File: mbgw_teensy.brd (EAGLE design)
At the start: 49 x 42 mm, 39 parts, among them IC1 MAX481CSA, Q1 MOSFET-N2N7002, Q2 MOSFET-N2N7002, Q3 MOSFET-N2N7002

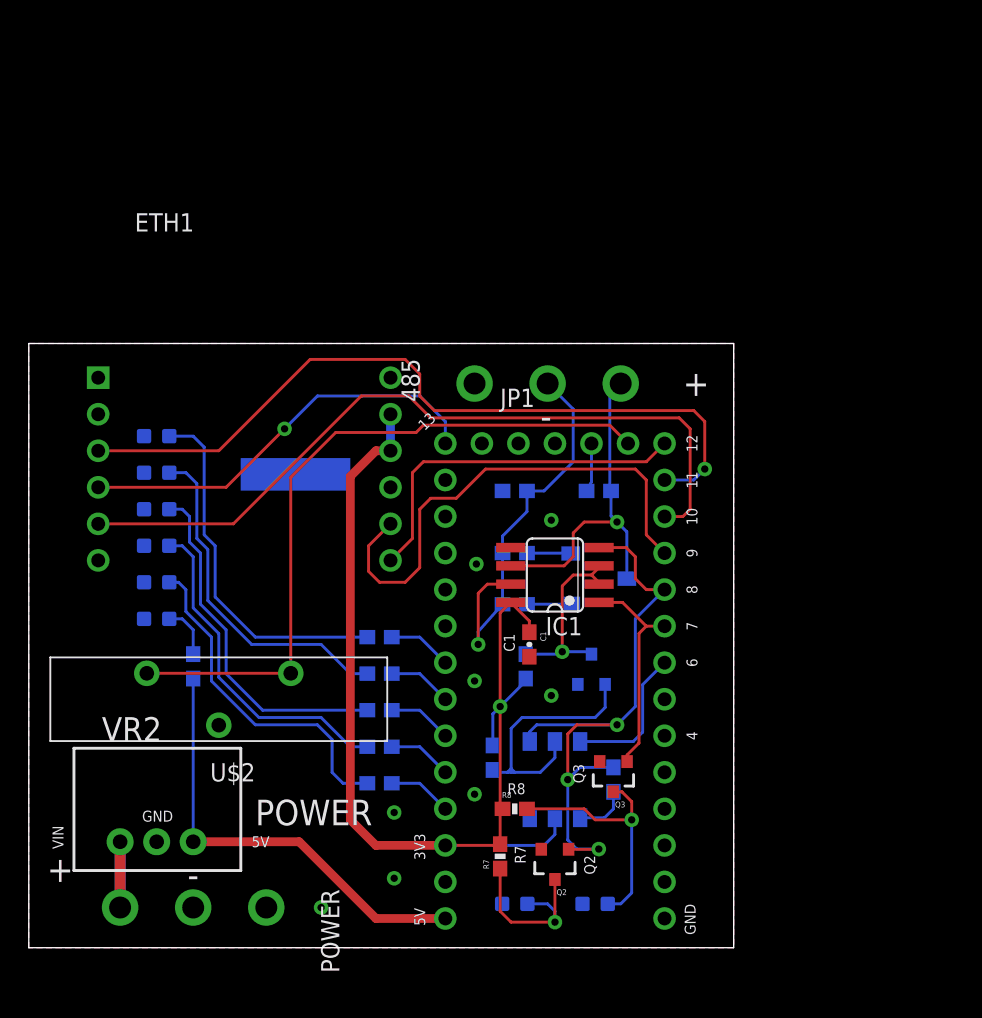
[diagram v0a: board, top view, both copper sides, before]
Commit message: 3/16/17, board with software switches for term resistor and tx/p6 control
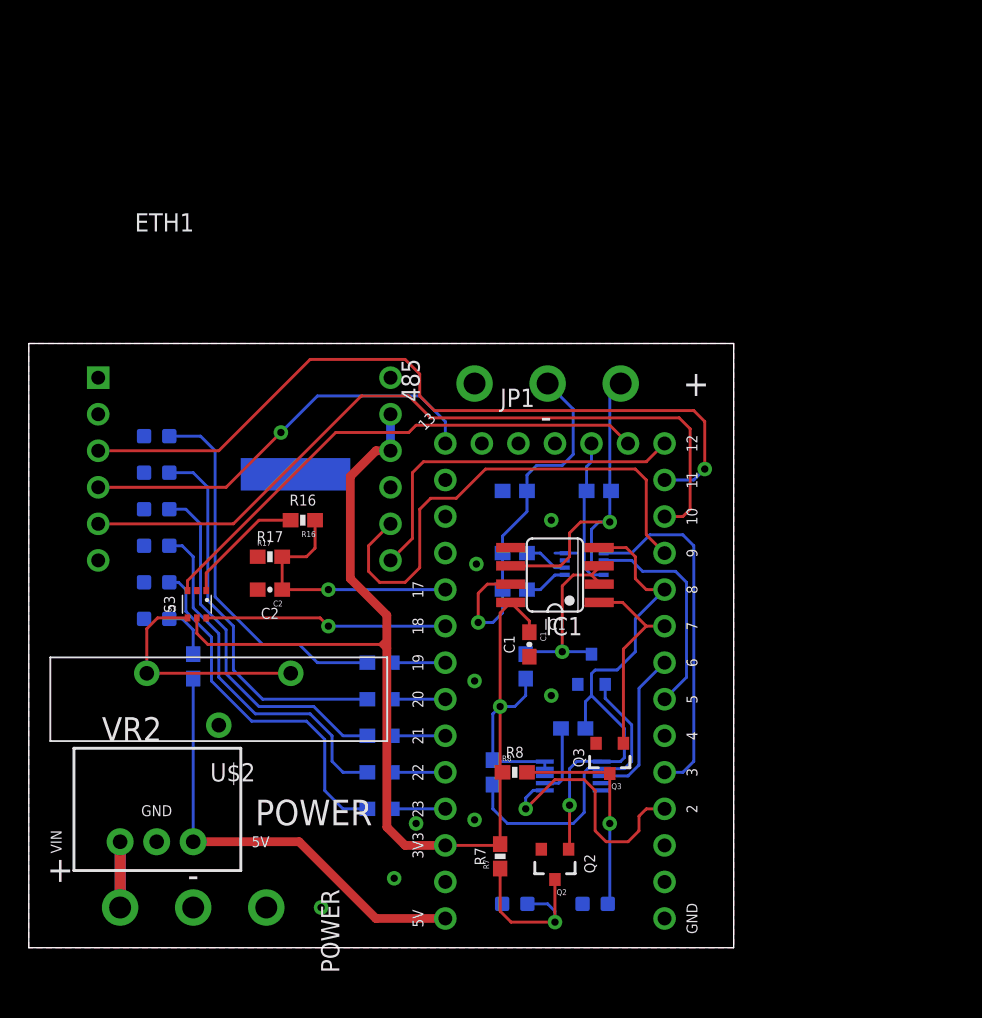
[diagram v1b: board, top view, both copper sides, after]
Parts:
- added C2: 273, SparkFun-Capacitors:0603-CAP
- added R16: 1K, SparkFun-Resistors:0603-RES
- added R17: 5.1K, SparkFun-Resistors:0603-RES
- added S3: NC7SB3157P6X, UPenn:1.25MM_6PIN
- S1: value DPDT_DIP_SMD -> MAX4525; device UPenn:DPDT_DIP_SMD -> UPenn:3MM_10PIN
- S2: value DIP_SWITCH_SPDT_N -> FSA3357K8X; device UPenn:SINGLE_DIP_SW_NEUT -> UPenn:2.3MM_8PIN
- moved R15 4.52 mm to (37.8, 15.2), turned to 0 degrees
- moved R8 2.54 mm to (33.8, 12.2)
- moved R3 1.78 mm to (24.4, 14.7)
- moved R4 1.78 mm to (24.4, 17.3)
- moved R1 1.78 mm to (24.4, 9.65)
- moved R2 1.78 mm to (24.4, 12.2)
- moved R5 1.78 mm to (24.4, 19.8)
- moved S2 1.44 mm to (38.6, 26.7)
- moved Q3 1.30 mm to (40.4, 13.2)
- moved S1 1.30 mm to (37.8, 11.9), turned to 270 degrees
- moved R10 1.02 mm to (32.3, 12.2)
- moved R13 1.02 mm to (33.8, 24.9)
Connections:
- new net N$30: R14.1, S2.P$2
- new net N$31: JP1.3, S2.P$5
- new net N$32: JP1.2, S1.P$6
- new net N$33: JP1.VBAT, S3.P$3
- new net N$35: C2.1, JP1.17, R16.1, R17.2
- new net N$37: R16.2, S3.P$1
- new net N$38: JP1.18, S3.P$6
- net 3.3V: now also S1.P$10, S1.P$9, S2.P$8, S3.P$5; no longer S1.2
- net GND: now also C2.2, R17.1, S1.P$4, S1.P$5, S2.P$4, S3.P$2
- net N$1: now also R15.2, S1.P$7; no longer R14.1, S2.2
- net N$12: now also S2.P$1; no longer S2.1
- net N$15: now also JP1.5, S2.P$6; no longer R15.2, S1.1
- net N$17: now also S1.P$1; no longer S1.6
- net N$2: now also S1.P$3; no longer S1.4
- net N$25: now also S2.P$7; no longer S2.3
- net N$26: now also S1.P$2; no longer S1.5
- net N$3: now also S3.P$4; no longer JP1.VBAT
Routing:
- net N$33: track 0.00 -> 36.3 mm
- net N$3: track 49.1 -> 16.2 mm
- net N$31: track 0.00 -> 24.5 mm
- net N$35: track 0.00 -> 18.1 mm, vias 0 -> 1
- net 3.3V: track 79.1 -> 97.2 mm
- net N$32: track 0.00 -> 17.8 mm, vias 0 -> 1
- net N$38: track 0.00 -> 16.9 mm, vias 0 -> 1
- net N$15: track 3.75 -> 15.2 mm
- net N$17: track 43.6 -> 34.5 mm, vias 3 -> 1
- net N$37: track 0.00 -> 8.61 mm
- net N$30: track 0.00 -> 3.05 mm
- net N$26: track 18.4 -> 21.3 mm
- net N$21: track 23.9 -> 26.7 mm
- net N$28: track 17.5 -> 15.2 mm
- net N$13: track 28.3 -> 26.3 mm
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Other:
- board text added: "17"
- board text added: "18"
- board text added: "19"
- board text added: "2"
- board text added: "20"
- board text added: "21"
- board text added: "22"
- board text added: "23"
- board text added: "3"
- board text added: "5"
- board text added: "BAT"
- board text added: "C2"
- board text added: "IC1"
- board text added: "R16"
- board text added: "R17"
- board text added: "Rev 3.0"
- board text added: "S3"
- board text removed: "120"
- board text removed: "270"
- board text removed: "D6_CTRL"
- board text removed: "Rev 2.1"
- board text removed: "TX_CTRL"

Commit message: 3/20/17, continue adjusting for stretched board
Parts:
- added MEM1: RM25C512CSOIC, UPenn:SO08
- added R18: 180, SparkFun-Resistors:0603-RES
- moved U$4 42.8 mm to (64.3, 42.9)
- moved 485 12.2 mm to (36.1, 51.4)
- moved ETH1 12.2 mm to (15.0, 45.5)
- moved BATT 4.32 mm to (8.89, 29.7)
- moved PWR 4.32 mm to (8.89, 27.2)
- moved RTCB 4.32 mm to (8.89, 32.3)
- moved SDB 4.32 mm to (8.89, 34.8)
- moved U$2 4.32 mm to (13.2, 21.6)
- moved POWER 4.32 mm to (11.4, 7.11)
- moved VR2 4.32 mm to (8.89, 11.7)
- moved EPW 4.32 mm to (8.89, 39.9)
- moved SDW 4.32 mm to (8.89, 37.3)
- moved S3 4.06 mm to (11.7, 27.9)
- moved R6 3.05 mm to (11.4, 16.5)
- moved R16 2.54 mm to (19.1, 32.3)
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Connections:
- new net N$34: R18.1, S2.P$3
- net 3.3V: now also MEM1.3, MEM1.7, MEM1.8
- net GND: now also MEM1.4
- net N$13: now also R18.2
- net N$6: now also MEM1.5
- net N$7: now also MEM1.2
- net N$8: now also MEM1.6
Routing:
- net N$5: track 53.4 -> 31.4 mm
- net N$8: track 29.0 -> 11.2 mm, vias 1 -> 0
- net N$6: track 53.9 -> 36.5 mm
- net N$33: track 36.3 -> 21.1 mm
- net N$18: track 25.1 -> 11.7 mm
- net N$20: track 25.2 -> 12.2 mm
- net N$25: track 23.9 -> 36.6 mm
- net N$13: track 26.3 -> 38.5 mm
- net N$19: track 25.3 -> 13.2 mm
- net VIN: track 9.14 -> 0.00 mm
- net N$37: track 8.61 -> 0.00 mm
- net N$7: track 25.1 -> 17.3 mm
- net N$14: track 3.67 -> 0.00 mm
- net N$34: track 0.00 -> 3.36 mm
- net N$11: track 26.2 -> 29.5 mm
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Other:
- board size 49 x 42 mm -> 49.5 x 58.5 mm
- board text added: "R18"

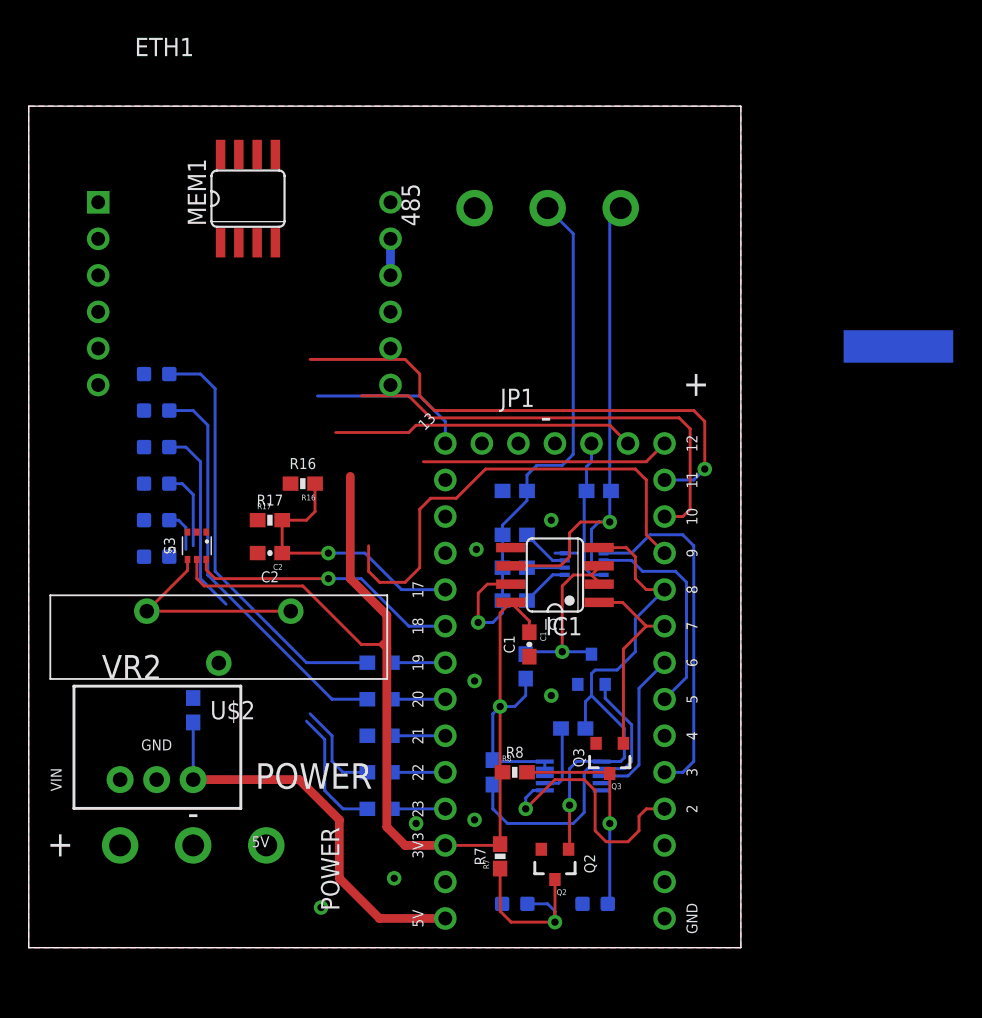
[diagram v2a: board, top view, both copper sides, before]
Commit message: 3/21/17, all chips connected, make sure everything visible
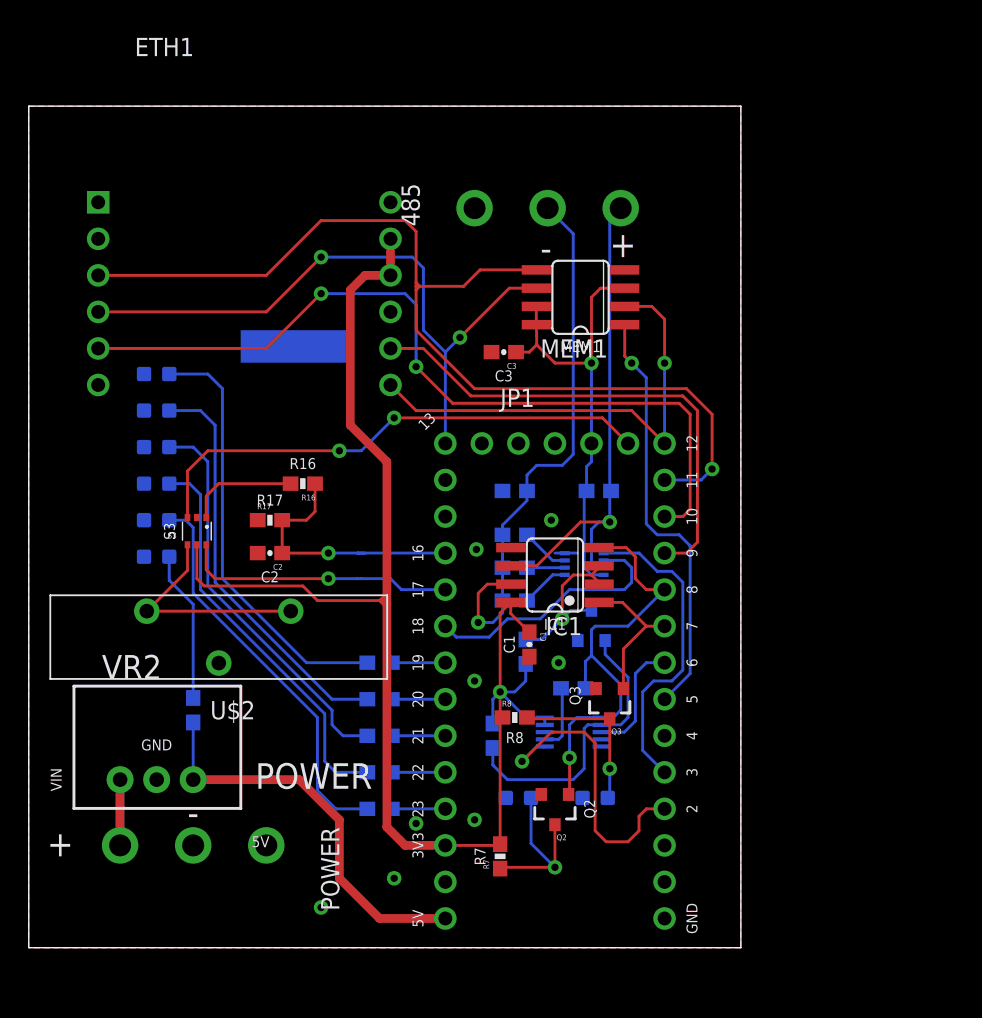
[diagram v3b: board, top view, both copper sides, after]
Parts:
- added C3: 104, SparkFun-Capacitors:0603-CAP
- moved U$4 41.9 mm to (22.4, 42.9)
- moved MEM1 24.1 mm to (38.4, 45.2), turned to 90 degrees
- moved LED1 7.37 mm to (34.0, 10.4)
- moved LED2 7.37 mm to (39.4, 10.4)
- moved Q3 3.81 mm to (40.4, 17.0)
- moved Q2 3.81 mm to (36.6, 9.65)
- moved R8 3.81 mm to (33.8, 16.0)
- moved Q1 3.05 mm to (39.1, 22.4)
- moved S1 3.05 mm to (37.8, 15.0)
- moved R15 2.79 mm to (37.8, 18.0)
- moved R10 2.54 mm to (32.3, 14.7)
- moved R9 1.02 mm to (34.5, 20.6)
- moved S3 1.02 mm to (11.7, 29.0)
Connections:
- new net N$36: JP1.5, MEM1.1
- net 3.3V: now also C3.1
- net GND: now also C3.2
- net N$15: now also JP1.18; no longer JP1.5
- net N$35: now also JP1.16; no longer JP1.17
- net N$38: now also JP1.17; no longer JP1.18
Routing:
- net 3.3V: track 95.5 -> 131.4 mm, vias 1 -> 2
- net N$8: track 11.2 -> 45.5 mm, vias 0 -> 2
- net N$6: track 36.5 -> 70.8 mm
- net N$36: track 0.00 -> 29.5 mm, vias 0 -> 1
- net N$5: track 31.4 -> 57.3 mm, vias 0 -> 2
- net N$18: track 11.7 -> 27.7 mm
- net N$20: track 12.2 -> 27.9 mm
- net N$7: track 17.3 -> 32.5 mm, vias 0 -> 1
- net N$33: track 21.1 -> 36.1 mm, vias 0 -> 2
- net N$19: track 13.2 -> 27.7 mm
- net N$14: track 0.00 -> 10.5 mm
- net VIN: track 0.00 -> 9.14 mm
- net N$37: track 0.00 -> 7.71 mm
- net N$17: track 34.5 -> 30.6 mm
- net N$16: track 14.0 -> 10.2 mm
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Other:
- board text added: "16"
- board text added: "C3"
- board text added: "MEM1"

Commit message: 3/22/17, gerber files made
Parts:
- added U$3: UPENN_SHIELD_.3_SILK, UPenn:UPENN_SHIELD_3_SILK
- moved R12 16.1 mm to (35.3, 47.8)
- moved R11 16.0 mm to (40.4, 47.8)
- moved U$4 6.35 mm to (22.4, 36.6)
- moved S2 2.34 mm to (39.1, 29.0)
- moved R13 2.29 mm to (33.8, 26.4)
- moved R14 2.29 mm to (33.8, 28.7)
- moved R18 2.29 mm to (33.8, 31.0)
- moved Q1 1.27 mm to (39.1, 23.6)
- moved R15 1.27 mm to (37.8, 19.3)
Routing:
- net 3.3V: track 131.4 -> 136.2 mm
- net N$32: track 21.1 -> 17.3 mm
- net N$25: track 35.6 -> 33.2 mm
- net N$13: track 38.5 -> 36.2 mm
- net N$31: track 22.1 -> 23.9 mm
- net N$26: track 20.4 -> 21.7 mm
- net N$1: track 4.65 -> 5.92 mm
- net GND: track 1.52 -> 0.51 mm, vias 8 -> 7
- net N$12: track 3.38 -> 4.40 mm
- net N$27: track 12.2 -> 11.5 mm
- net N$17: track 30.6 -> 31.4 mm
- net N$33: track 36.1 -> 36.6 mm
- net N$34: track 3.36 -> 3.87 mm
- net N$30: track 2.63 -> 3.13 mm
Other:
- board text added: "Rev 4.0"
- board text removed: "Rev 3.0"

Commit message: 3/23/17, added BOM
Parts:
- RX, TX: value (none) -> YLW
- renumbered LED1 to TX, LED2 to RX
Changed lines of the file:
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@@
 <element name="R14" library="SparkFun-Resistors" package="0603-RES" value="270" x="33.782" y="28.702" rot="MR0"/>
 <element name="C1" library="SparkFun-Capacitors" package="0603-CAP" value="104" x="34.798" y="21.082" rot="R270"/>
-<element name="LED1" library="SparkFun-LED" package="LED-0603" value="" x="34.036" y="10.414" rot="MR270"/>
-<element name="LED2" library="SparkFun-LED" package="LED-0603" value="" x="39.37" y="10.414" rot="MR270"/>
+<element name="TX" library="SparkFun-LED" package="LED-0603" value="YLW" x="34.036" y="10.414" rot="MR270"/>
+<element name="RX" library="SparkFun-LED" package="LED-0603" value="YLW" x="39.37" y="10.414" rot="MR270"/>
 <element name="IC1" library="maxim" package="SO08" value="MAX481CSA" x="36.576" y="25.908" rot="R90">
 <attribute name="MF" value="MAXIM" x="36.576" y="25.908" size="1.778" layer="27" rot="R90" display="off"/>
@@
 <contactref element="Q1" pad="2"/>
 <contactref element="PWR" pad="C"/>
-<contactref element="LED1" pad="C"/>
-<contactref element="LED2" pad="C"/>
+<contactref element="TX" pad="C"/>
+<contactref element="RX" pad="C"/>
 <contactref element="Q2" pad="2"/>
 <contactref element="Q3" pad="2"/>
@@
 </signal>
 <signal name="N$28">
-<contactref element="LED2" pad="A"/>
+<contactref element="RX" pad="A"/>
 <contactref element="R8" pad="2"/>
 <contactref element="Q3" pad="3"/>
@@
 <contactref element="Q2" pad="3"/>
 <contactref element="R7" pad="1"/>
-<contactref element="LED1" pad="A"/>
+<contactref element="TX" pad="A"/>
 <via x="36.576" y="5.588" extent="1-16" drill="0.508"/>
 <wire x1="36.576" y1="5.588" x2="36.576" y2="8.552" width="0.2032" layer="1"/>

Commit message: 3/23/17, fram instead of eeprom memory
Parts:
- MEM1: value RM25C512CSOIC -> MB85RS256BPNFSOIC
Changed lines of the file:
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@@
 <layers>
 <layer number="1" name="Top" color="4" fill="1" visible="yes" active="yes"/>
-<layer number="16" name="Bottom" color="1" fill="1" visible="yes" active="yes"/>
+<layer number="16" name="Bottom" color="1" fill="1" visible="no" active="yes"/>
 <layer number="17" name="Pads" color="2" fill="1" visible="yes" active="yes"/>
 <layer number="18" name="Vias" color="2" fill="1" visible="yes" active="yes"/>
@@
 <layer number="20" name="Dimension" color="15" fill="1" visible="yes" active="yes"/>
 <layer number="21" name="tPlace" color="7" fill="1" visible="yes" active="yes"/>
-<layer number="22" name="bPlace" color="7" fill="1" visible="yes" active="yes"/>
+<layer number="22" name="bPlace" color="7" fill="1" visible="no" active="yes"/>
 <layer number="23" name="tOrigins" color="15" fill="1" visible="yes" active="yes"/>
-<layer number="24" name="bOrigins" color="15" fill="1" visible="yes" active="yes"/>
+<layer number="24" name="bOrigins" color="15" fill="1" visible="no" active="yes"/>
 <layer number="25" name="tNames" color="7" fill="1" visible="no" active="yes"/>
 <layer number="26" name="bNames" color="7" fill="1" visible="no" active="yes"/>
@@
 <layer number="28" name="bValues" color="7" fill="1" visible="no" active="yes"/>
 <layer number="29" name="tStop" color="7" fill="3" visible="yes" active="yes"/>
-<layer number="30" name="bStop" color="7" fill="6" visible="yes" active="yes"/>
+<layer number="30" name="bStop" color="7" fill="6" visible="no" active="yes"/>
 <layer number="31" name="tCream" color="7" fill="4" visible="no" active="yes"/>
 <layer number="32" name="bCream" color="7" fill="5" visible="no" active="yes"/>
@@
 <layer number="38" name="bTest" color="7" fill="1" visible="no" active="yes"/>
 <layer number="39" name="tKeepout" color="4" fill="11" visible="yes" active="yes"/>
-<layer number="40" name="bKeepout" color="1" fill="11" visible="yes" active="yes"/>
+<layer number="40" name="bKeepout" color="1" fill="11" visible="no" active="yes"/>
 <layer number="41" name="tRestrict" color="4" fill="10" visible="yes" active="yes"/>
-<layer number="42" name="bRestrict" color="1" fill="10" visible="yes" active="yes"/>
+<layer number="42" name="bRestrict" color="1" fill="10" visible="no" active="yes"/>
 <layer number="43" name="vRestrict" color="2" fill="10" visible="yes" active="yes"/>
 <layer number="44" name="Drills" color="7" fill="1" visible="no" active="yes"/>
@@
 <layer number="104" name="Name" color="16" fill="1" visible="yes" active="yes"/>
 <layer number="105" name="tPlate" color="7" fill="1" visible="yes" active="yes"/>
-<layer number="106" name="bPlate" color="7" fill="1" visible="yes" active="yes"/>
+<layer number="106" name="bPlate" color="7" fill="1" visible="no" active="yes"/>
 <layer number="107" name="Crop" color="7" fill="1" visible="yes" active="yes"/>
 <layer number="108" name="tplace-old" color="10" fill="1" visible="yes" active="yes"/>
@@
 <layer number="118" name="Rect_Pads" color="7" fill="1" visible="yes" active="yes"/>
 <layer number="121" name="_tsilk" color="7" fill="1" visible="yes" active="yes"/>
-<layer number="122" name="_bsilk" color="7" fill="1" visible="yes" active="yes"/>
+<layer number="122" name="_bsilk" color="7" fill="1" visible="no" active="yes"/>
 <layer number="123" name="tTestmark" color="7" fill="1" visible="yes" active="yes"/>
-<layer number="124" name="bTestmark" color="7" fill="1" visible="yes" active="yes"/>
+<layer number="124" name="bTestmark" color="7" fill="1" visible="no" active="yes"/>
 <layer number="125" name="_tNames" color="7" fill="1" visible="yes" active="yes"/>
-<layer number="126" name="_bNames" color="7" fill="1" visible="yes" active="yes"/>
+<layer number="126" name="_bNames" color="7" fill="1" visible="no" active="yes"/>
 <layer number="127" name="_tValues" color="7" fill="1" visible="yes" active="yes"/>
-<layer number="128" name="_bValues" color="7" fill="1" visible="yes" active="yes"/>
+<layer number="128" name="_bValues" color="7" fill="1" visible="no" active="yes"/>
 <layer number="129" name="Mask" color="7" fill="1" visible="yes" active="yes"/>
 <layer number="131" name="tAdjust" color="7" fill="1" visible="yes" active="yes"/>
-<layer number="132" name="bAdjust" color="7" fill="1" visible="yes" active="yes"/>
+<layer number="132" name="bAdjust" color="7" fill="1" visible="no" active="yes"/>
 <layer number="144" name="Drill_legend" color="7" fill="1" visible="yes" active="yes"/>
 <layer number="150" name="Notes" color="7" fill="1" visible="yes" active="yes"/>
 <layer number="151" name="HeatSink" color="7" fill="1" visible="yes" active="yes"/>
-<layer number="152" name="_bDocu" color="7" fill="1" visible="yes" active="yes"/>
+<layer number="152" name="_bDocu" color="7" fill="1" visible="no" active="yes"/>
 <layer number="153" name="FabDoc1" color="7" fill="1" visible="yes" active="yes"/>
 <layer number="154" name="FabDoc2" color="7" fill="1" visible="yes" active="yes"/>
@@
 <element name="R17" library="SparkFun-Resistors" package="0603-RES" value="5.1K" x="16.764" y="29.718"/>
 <element name="C2" library="SparkFun-Capacitors" package="0603-CAP" value="273" x="16.764" y="27.432" rot="R180"/>
-<element name="MEM1" library="UPenn" package="SO08" value="RM25C512CSOIC" x="38.354" y="45.212" rot="R90"/>
+<element name="MEM1" library="UPenn" package="SO08" value="MB85RS256BPNFSOIC" x="38.354" y="45.212" rot="R90"/>
 <element name="R18" library="SparkFun-Resistors" package="0603-RES" value="180" x="33.782" y="30.988" rot="MR0"/>
 <element name="C3" library="SparkFun-Capacitors" package="0603-CAP" value="104" x="33.02" y="41.402" rot="R180"/>
